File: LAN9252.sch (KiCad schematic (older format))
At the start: 2 parts

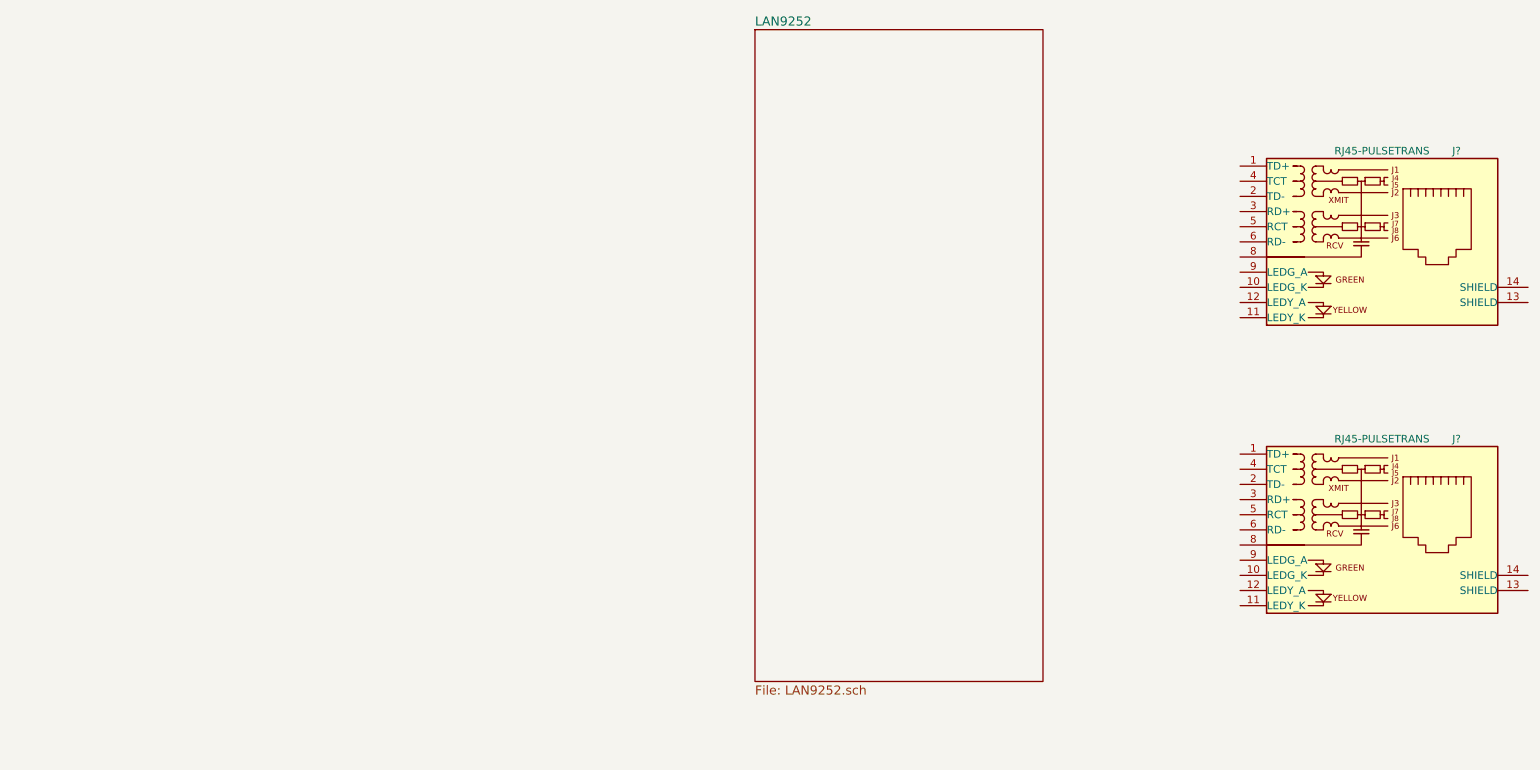
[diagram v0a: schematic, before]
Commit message: Add new sheet LAN9252
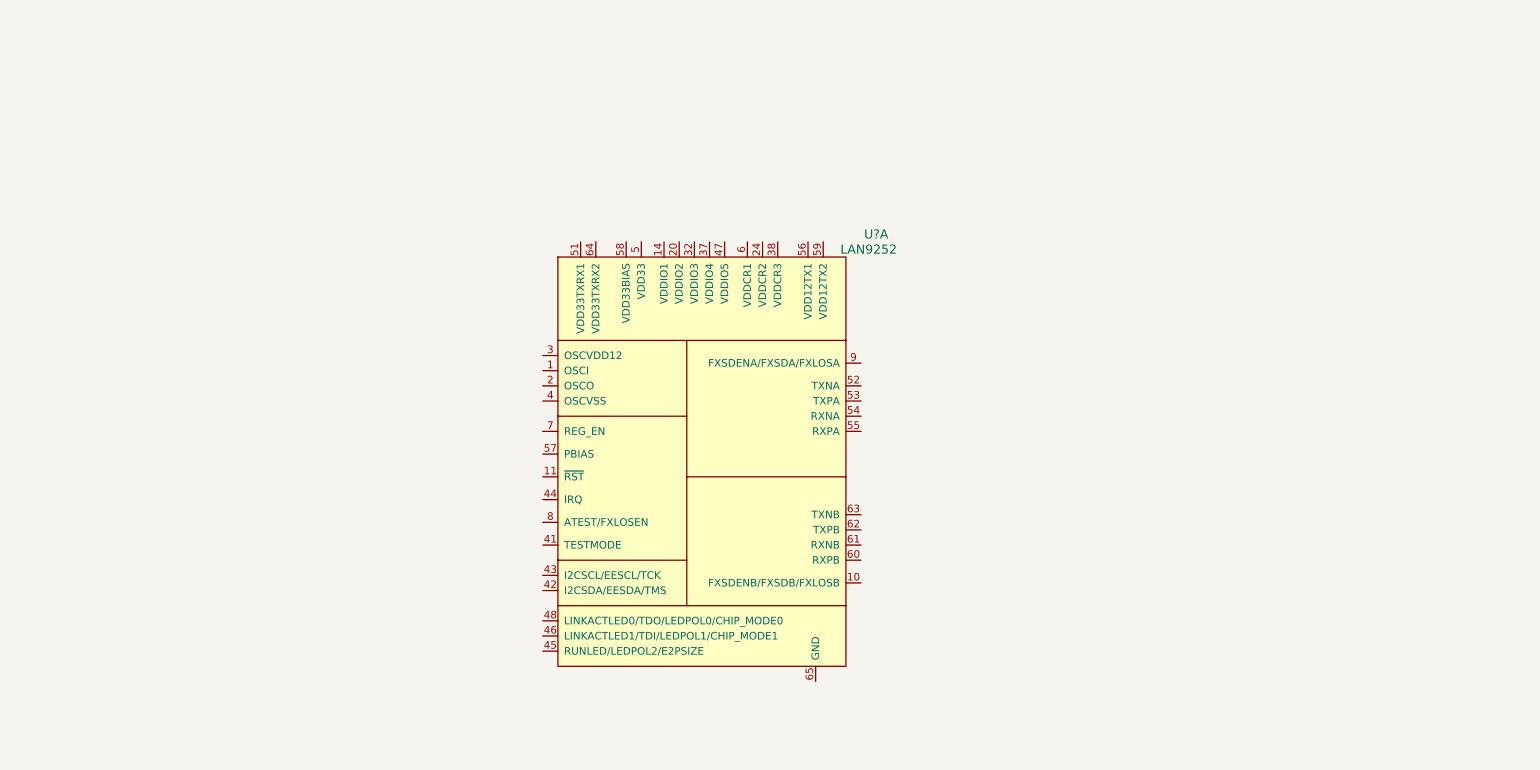
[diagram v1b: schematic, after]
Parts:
- removed J? (x2): RJ45-PULSETRANS, symbol RJ45-PULSETRANS
- added U?: LAN9252, symbol LAN9252
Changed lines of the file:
@@
 $Descr A4 11693 8268
 encoding utf-8
-Sheet 1 2
+Sheet 2 2
 Title ""
 Date ""
@@
 $EndDescr
 $Comp
-L RJ45-PULSETRANS J?
-U 1 1 59222621
-P 10150 5050
-F 0 "J?" H 10250 5650 50  0000 L CNN
-F 1 "RJ45-PULSETRANS" H 10100 5650 50  0000 R CNN
-F 2 "" H 10150 5050 50  0001 C CNN
-F 3 "" H 10150 5050 50  0001 C CNN
-	1    10150 5050
+L LAN9252 U?
+U 1 1 592227B1
+P 6250 3250
+F 0 "U?" H 6450 3400 60  0000 C CNN
+F 1 "LAN9252" H 6400 3300 60  0000 C CNN
+F 2 "" H 5000 2200 60  0001 C CNN
+F 3 "" H 5000 2200 60  0001 C CNN
+	1    6250 3250
 	1    0    0    -1
 $EndComp
-$Comp
-L RJ45-PULSETRANS J?
-U 1 1 592226C0
-P 10150 3150
-F 0 "J?" H 10250 3750 50  0000 L CNN
-F 1 "RJ45-PULSETRANS" H 10100 3750 50  0000 R CNN
-F 2 "" H 10150 3150 50  0001 C CNN
-F 3 "" H 10150 3150 50  0001 C CNN
-	1    10150 3150
-	1    0    0    -1
-$EndComp
-$Sheet
-S 5650 1750 1900 4300
-U 5922279E
-F0 "LAN9252" 60
-F1 "LAN9252.sch" 60
-$EndSheet
 $EndSCHEMATC

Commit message: LAN9252まわりの配線した
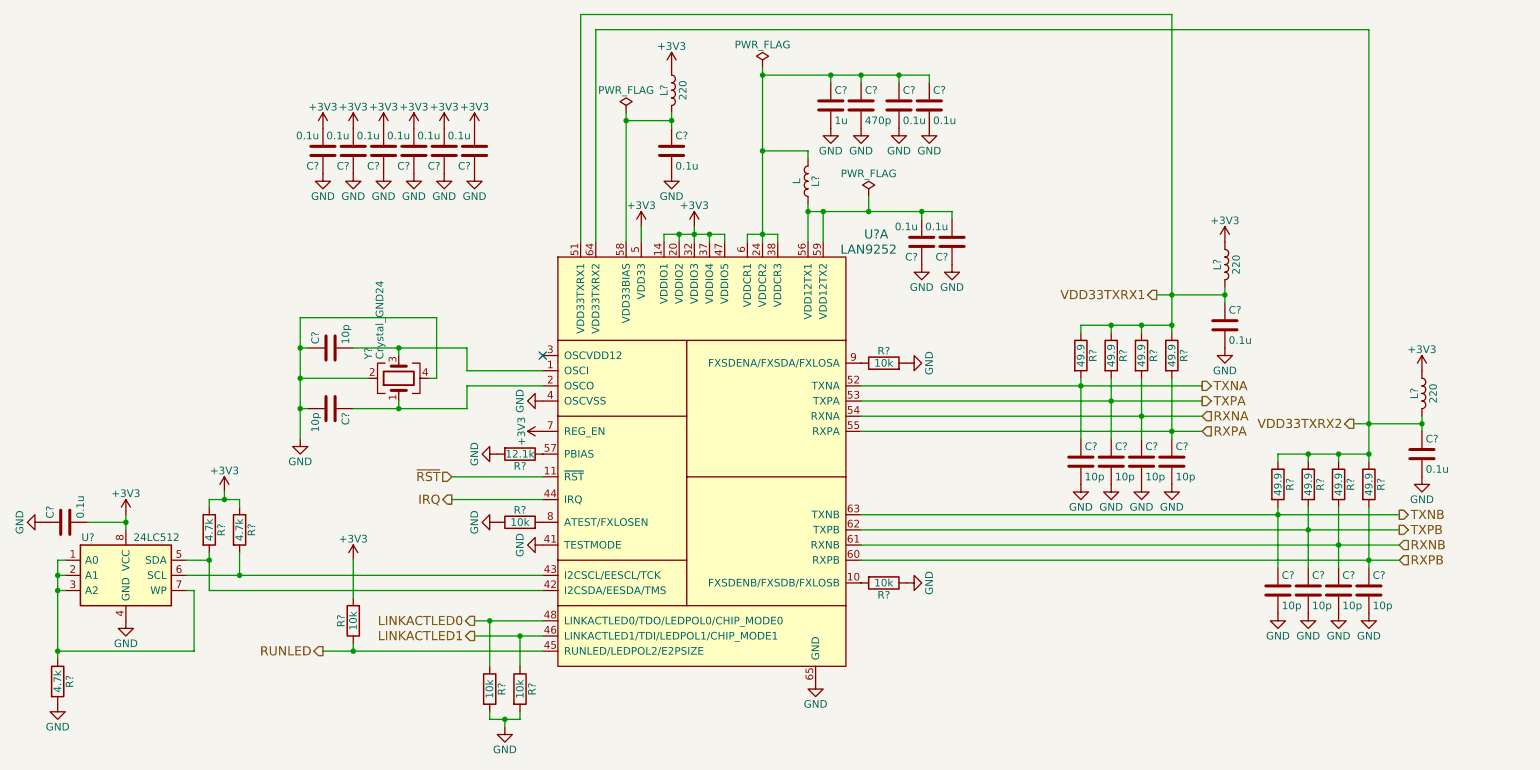
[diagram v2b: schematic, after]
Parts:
- added C? (x14): 0.1u, symbol C
- added C? (x10): 10p, symbol C
- added C?: 1u, symbol C
- added C?: 470p, symbol C
- added L?: L, symbol L
- added L? (x3): 220, symbol L
- added R? (x6): 10k, symbol R
- added R? (x8): 49.9, symbol R
- added R?: 12.1k, symbol R
- added R? (x3): 4.7k, symbol R
- added U?: 24LC512, Housings_SOIC:SOIC-8_3.9x4.9mm_Pitch1.27mm, symbol 24LC512
- added Y?: Crystal_GND24, symbol Crystal_GND24
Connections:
- net at U?.1 (OSCI): now also C?.2, Y?.3
- net at U?.10 (FXSDENB/FXSDB/FXLOSB): now also R?.2
- net ~RST: now reaches U?.11 (~RST)
- net +3V3: now reaches U?.14 (VDDIO1)
- net +3V3: now also U?.20 (VDDIO2), U?.32 (VDDIO3), U?.37 (VDDIO4), U?.47 (VDDIO5), U?.5 (VDD33), U?.7 (REG_EN), C?.2, C?.2, C?.2, C?.2, C?.2, C?.2, C?.2, L?.1, L?.1, L?.1, R?.1, R?.1, R?.2, U?.8 (VCC)
- net at U?.2 (OSCO): now also C?.1, Y?.1
- net at U?.24 (VDDCR2): now also U?.38 (VDDCR3), U?.6 (VDDCR1), C?.1, C?.1, C?.1, C?.1, L?.2
- net GND: now reaches U?.4 (OSCVSS)
- net GND: now also U?.41 (TESTMODE), U?.65 (GND), C?.1, C?.1, C?.1, C?.1, C?.1, C?.1, C?.1, C?.1, C?.1, C?.1, C?.2, C?.2, C?.2, C?.2, C?.2, C?.2, C?.2, C?.2, C?.2, C?.2, C?.2, C?.2, C?.2, C?.2, C?.2, C?.2, R?.1, R?.1, R?.2, R?.2, R?.2, R?.2, R?.2, U?.4 (GND), Y?.2, Y?.4
- net at U?.42 (I2CSDA/EESDA/TMS): now also R?.2, U?.5 (SDA)
- net at U?.43 (I2CSCL/EESCL/TCK): now also R?.2, U?.6 (SCL)
- net IRQ: now reaches U?.44 (IRQ)
- net RUNLED: now reaches U?.45 (RUNLED/LEDPOL2/E2PSIZE)
- net RUNLED: now also R?.1
- net LINKACTLED1: now reaches U?.46 (LINKACTLED1/TDI/LEDPOL1/CHIP_MODE1)
- net LINKACTLED1: now also R?.1
- net LINKACTLED0: now reaches U?.48 (LINKACTLED0/TDO/LEDPOL0/CHIP_MODE0)
- net LINKACTLED0: now also R?.1
- net VDD33TXRX1: now reaches U?.51 (VDD33TXRX1)
- net VDD33TXRX1: now also C?.1, L?.2, R?.1, R?.1, R?.1, R?.1
- net TXNA: now reaches U?.52 (TXNA)
- net TXNA: now also C?.1, R?.2
- net TXPA: now reaches U?.53 (TXPA)
- net TXPA: now also C?.1, R?.2
- net RXNA: now reaches U?.54 (RXNA)
- net RXNA: now also C?.1, R?.2
- net RXPA: now reaches U?.55 (RXPA)
- net RXPA: now also C?.1, R?.2
- net at U?.56 (VDD12TX1): now also U?.59 (VDD12TX2), C?.2, C?.2, L?.1
- net at U?.57 (PBIAS): now also R?.1
- net at U?.58 (VDD33BIAS): now also C?.1, L?.2
- net RXPB: now reaches U?.60 (RXPB)
- net RXPB: now also C?.1, R?.2
- net RXNB: now reaches U?.61 (RXNB)
- net RXNB: now also C?.1, R?.2
- net TXPB: now reaches U?.62 (TXPB)
- net TXPB: now also C?.1, R?.2
- net TXNB: now reaches U?.63 (TXNB)
- net TXNB: now also C?.1, R?.2
- net VDD33TXRX2: now reaches U?.64 (VDD33TXRX2)
- net VDD33TXRX2: now also C?.1, L?.2, R?.1, R?.1, R?.1, R?.1
- net at U?.8 (ATEST/FXLOSEN): now also R?.2
- net at U?.9 (FXSDENA/FXSDA/FXLOSA): now also R?.1
- new net: R?.1, U?.1 (A0), U?.2 (A1), U?.3 (A2), U?.7 (WP)
- no-connect marks 0 -> 1

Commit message: スイッチ，LEDの配線 電源回路追加 アノテーション
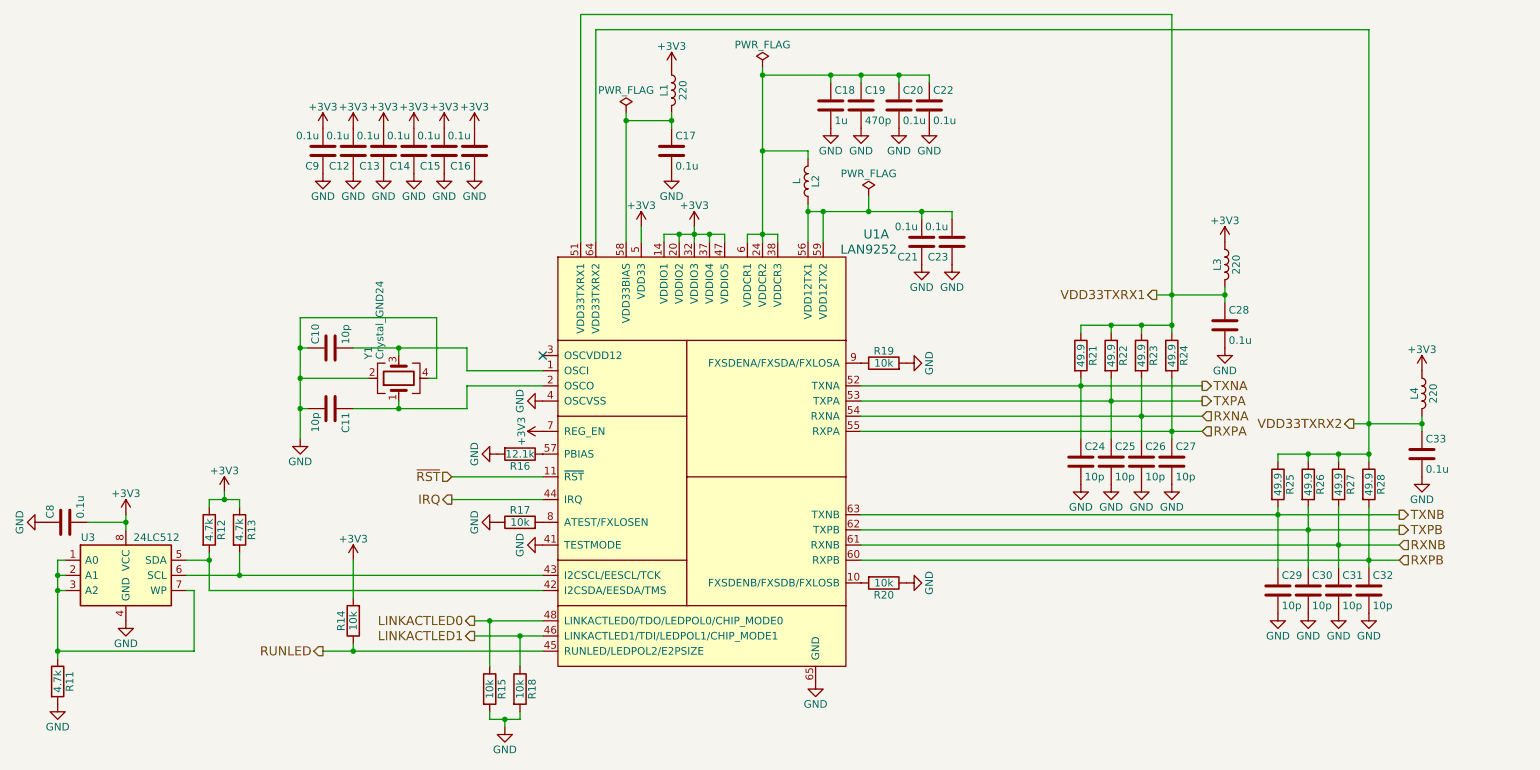
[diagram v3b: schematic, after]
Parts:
- gave numbers to parts that had none: 51

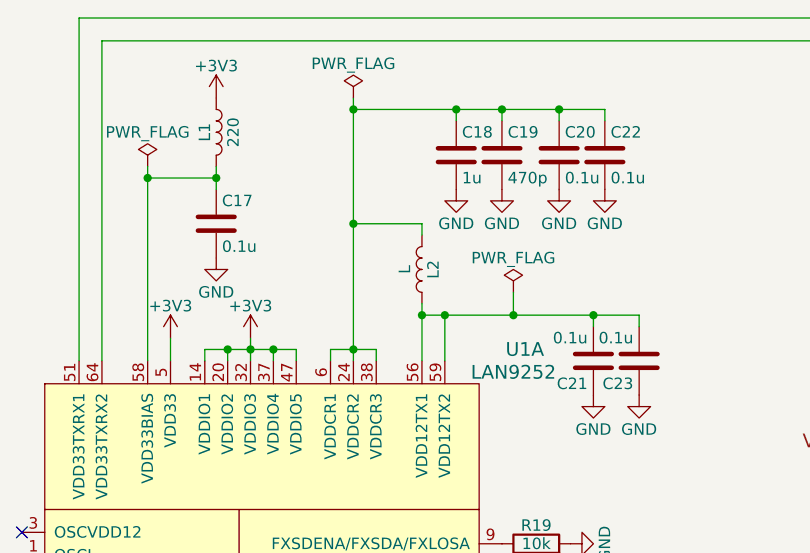
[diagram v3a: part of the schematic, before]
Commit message: フットプリント割当 基板作成開始
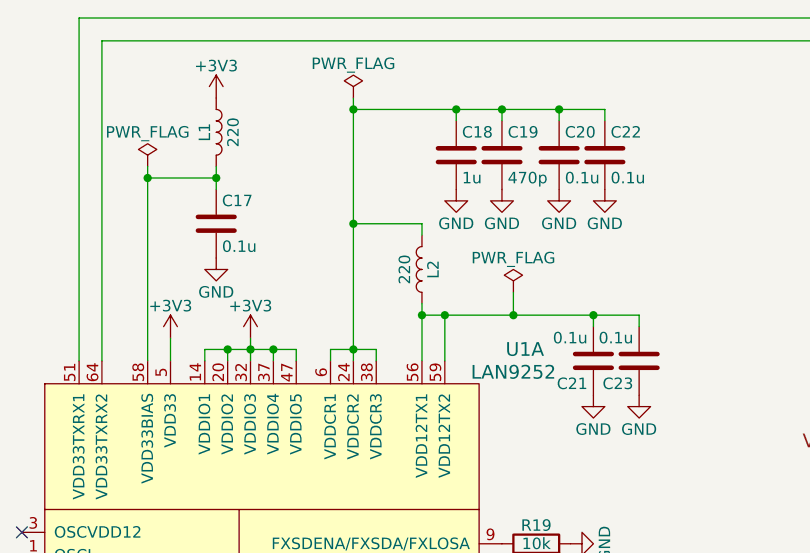
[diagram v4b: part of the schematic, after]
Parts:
- C10, C11, C12, C13, C14, C15, C16, C17, C18, C19, C20, C21, C22, C23, C24, C25, C26, C27, C28, C29, C30, C31, C32, C33, C8, C9, L1, L3, L4: footprint (none) -> Capacitors_SMD:C_0603
- L2: value L -> 220; footprint (none) -> Capacitors_SMD:C_0603
- R11, R12, R13, R14, R15, R16, R17, R18, R19, R20, R21, R22, R23, R24, R25, R26, R27, R28: footprint (none) -> Resistors_SMD:R_0603
- U1: footprint (none) -> Housings_DFN_QFN:QFN-64-1EP_9x9mm_Pitch0.5mm_LAN9252
- Y1: footprint (none) -> Crystals:Crystal_SMD_Abracon_ABM8G-4pin_3.2x2.5mm
